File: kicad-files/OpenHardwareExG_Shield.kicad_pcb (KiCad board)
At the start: 4 copper layers, 125.1 x 59.7 mm, 195 parts, among them P1 CONN_1, P10 CONN_18, P11 CONN_1, P12 CONN_1, P13 CONN_1, P14 CONN_1, P15 CONN_1, P16 CONN_1, P17 CONN_1, P18 CONN_1, P19 ARDUINO_SHIELD, P2 CONN_1, P20 CONN_3X2, P21 CONN_3X2, P22 CONN_7, P23 CONN_1, P24 CONN_1, P25 CONN_1, P26 CONN_1, P27 CONN_1, P28 CONN_1, P29 CONN_1, P3 CONN_1, P30 CONN_1, P31 CONN_1, P32 CONN_1, P33 CONN_1, P34 CONN_1, P35 CONN_1, P36 CONN_1, P37 CONN_1, P38 CONN_1, P39 CONN_1, P4 CONN_1, P40 CONN_1, P41 CONN_1, P42 CONN_1, P43 CONN_1, P44 CONN_1, P45 CONN_1, P46 CONN_1, P47 CONN_1, P48 CONN_1, P49 CONN_1, P5 CONN_1, P50 CONN_1, P51 CONN_1, P52 CONN_1, P53 CONN_1, P54 CONN_1, P55 CONN_1, P6 CONN_1, P7 CONN_1, P8 CONN_1, P9 CONN_1, U1 ADS1299, U2 BT1308W-600D, U3 TL431BIDBZR, U4 873-AAT3220IGY-33T1, U5 ADUM6000, U6 SI8663, U7 74LS02, U8 74LS00, U9 74LS125

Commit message: add rev. 0.0 to silk screen
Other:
- board text added: "rev. 0.0"
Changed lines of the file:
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@@
     (area 59.004999 28.0083 184.7167 91.2876)
     (thickness 1.6)
-    (drawings 51)
+    (drawings 53)
     (tracks 1163)
     (zones 0)
@@
     (22 B.Mask user)
     (23 F.Mask user)
-    (24 Dwgs.User user)
-    (25 Cmts.User user)
-    (26 Eco1.User user)
-    (27 Eco2.User user)
+    (24 Dwgs.User user hide)
+    (25 Cmts.User user hide)
+    (26 Eco1.User user hide)
+    (27 Eco2.User user hide)
     (28 Edge.Cuts user)
   )
@@
     (pad_to_mask_clearance 0)
     (aux_axis_origin 0 0)
-    (visible_elements 7FFFFFBF)
+    (visible_elements 7FFFFF3F)
     (pcbplotparams
-      (layerselection 284983303)
+      (layerselection 3145728)
       (usegerberextensions true)
       (excludeedgelayer true)
@@
     )
   )
+  (gr_text "rev. 0.0" (at 154.94 78.74) (layer F.SilkS)
+    (effects (font (size 1.016 1.016) (thickness 0.2032)))
+  )
+  (gr_text "rev. 0.0" (at 154.94 78.74) (layer B.SilkS)
+    (effects (font (size 1.016 1.016) (thickness 0.2032)) (justify mirror))
+  )
   (gr_text "Licensed under CERN OHL v.1.2 or later\nhttp://ohwr.org/cernohl" (at 99.314 85.852) (layer B.SilkS)

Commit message: replace triac, new manufacture part number does not include a comma
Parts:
- U2: value BT1308W-600D -> Z0109MNT1G
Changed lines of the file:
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@@
       (effects (font (size 0.6 0.6) (thickness 0.127)))
     )
-    (fp_text value BT1308W-600D (at 0 0.762 180) (layer F.SilkS) hide
+    (fp_text value Z0109MNT1G (at 0 0.762 180) (layer F.SilkS) hide
       (effects (font (size 1.016 1.016) (thickness 0.2032)))
     )

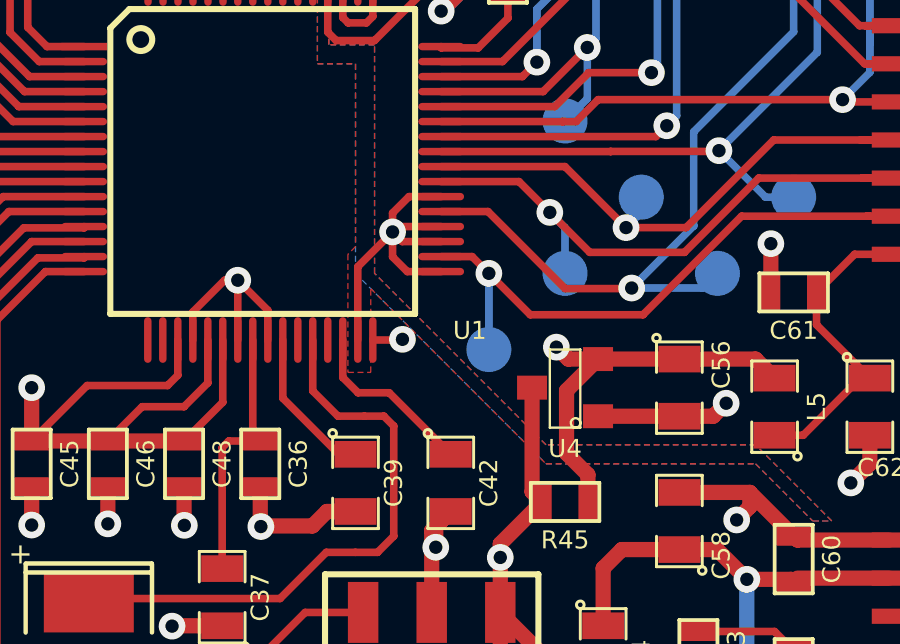
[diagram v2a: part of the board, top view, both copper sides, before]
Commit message: fixup PCB to tie ~PWDN~ and ~RESET~ to 3.3V_ISO
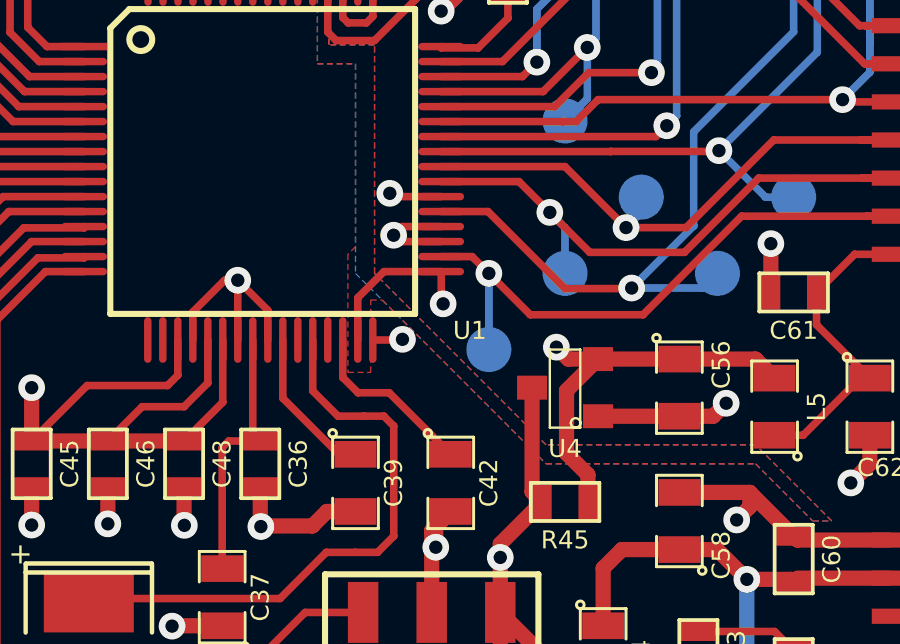
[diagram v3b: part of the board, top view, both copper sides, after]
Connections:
- U1 pad 35: AGND -> /3.3V_ISO
- U1 pad 36: AGND -> /3.3V_ISO
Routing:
- net AGND: track 162.5 -> 157.3 mm, vias 63 -> 64
- net /3.3V_ISO: track 20.2 -> 23.5 mm, vias 3 -> 4
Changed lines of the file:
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@@
     (thickness 1.6)
     (drawings 53)
-    (tracks 1163)
+    (tracks 1164)
     (zones 0)
     (modules 195)
@@
   (setup
     (last_trace_width 0.254)
+    (user_trace_width 0.254)
     (trace_clearance 0.2032)
     (zone_clearance 0.254)
@@
     (pad_to_mask_clearance 0)
     (aux_axis_origin 0 0)
-    (visible_elements 7FFFFF3F)
+    (visible_elements 7FFFF73F)
     (pcbplotparams
       (layerselection 3145728)
@@
   (net 101 N-000008)
   (net 102 N-0000080)
-  (net 103 N-0000088)
+  (net 103 N-0000087)
   (net 104 N-0000095)
   (net 105 VCC)
@@
     (add_net N-000008)
     (add_net N-0000080)
+    (add_net N-0000087)
     (add_net N-0000095)
   )
@@
     (add_net GND)
     (add_net N-00000107)
-    (add_net N-0000088)
     (add_net VCC)
   )
@@
     (pad 35 smd oval (at 2.75082 -6.0325 270) (size 0.24892 1.524)
       (layers F.Cu F.Paste F.Mask)
-      (net 57 AGND)
+      (net 4 /3.3V_ISO)
     )
     (pad 36 smd oval (at 2.25044 -6.0325 270) (size 0.24892 1.524)
       (layers F.Cu F.Paste F.Mask)
-      (net 57 AGND)
+      (net 4 /3.3V_ISO)
     )
     (pad 37 smd oval (at 1.75006 -6.0325 270) (size 0.24892 1.524)
@@
     (pad 1 smd rect (at -4.445 5.08 90) (size 0.508 1.143)
       (layers F.Cu F.Paste F.Mask)
-      (net 103 N-0000088)
+      (net 103 N-0000087)
     )
     (pad 2 smd rect (at -3.175 5.08 90) (size 0.508 1.143)
@@
     (pad 6 smd rect (at 1.905 5.08 90) (size 0.508 1.143)
       (layers F.Cu F.Paste F.Mask)
-      (net 103 N-0000088)
+      (net 103 N-0000087)
     )
     (pad 7 smd rect (at 3.175 5.08 90) (size 0.508 1.143)
       (layers F.Cu F.Paste F.Mask)
-      (net 103 N-0000088)
+      (net 103 N-0000087)
     )
     (pad 8 smd rect (at 4.445 5.08 90) (size 0.508 1.143)
@@
     (pad 1 smd rect (at -0.9525 0 90) (size 0.889 1.397)
       (layers F.Cu F.Paste F.Mask)
-      (net 103 N-0000088)
+      (net 103 N-0000087)
     )
     (pad 2 smd rect (at 0.9525 0 90) (size 0.889 1.397)
@@
     (pad 1 smd rect (at -0.9525 0 90) (size 0.889 1.397)
       (layers F.Cu F.Paste F.Mask)
-      (net 103 N-0000088)
+      (net 103 N-0000087)
     )
     (pad 2 smd rect (at 0.9525 0 90) (size 0.889 1.397)
@@
     (pad 1 smd rect (at -0.9525 0) (size 0.889 1.397)
       (layers F.Cu F.Paste F.Mask)
-      (net 103 N-0000088)
+      (net 103 N-0000087)
     )
     (pad 2 smd rect (at 0.9525 0) (size 0.889 1.397)
@@
     (pad 1 smd rect (at -0.762 0 90) (size 0.635 1.143)
       (layers F.Cu F.Paste F.Mask)
-      (net 103 N-0000088)
+      (net 103 N-0000087)
     )
     (pad 2 smd rect (at 0.762 0 90) (size 0.635 1.143)
@@
     (pad 1 smd rect (at -0.762 0 90) (size 0.635 1.143)
       (layers F.Cu F.Paste F.Mask)
-      (net 103 N-0000088)
+      (net 103 N-0000087)
     )
     (pad 2 smd rect (at 0.762 0 90) (size 0.635 1.143)
@@
   (segment (start 175.26 63.5) (end 177.8 60.96) (width 0.508) (layer B.Cu) (net 3))
   (segment (start 177.8 60.96) (end 180.34 60.96) (width 0.508) (layer B.Cu) (net 3))
+  (segment (start 100.0125 62.44082) (end 98.63582 62.44082) (width 0.254) (layer F.Cu) (net 4))
+  (segment (start 98.63582 62.44082) (end 98.425 62.23) (width 0.254) (layer F.Cu) (net 4))
+  (segment (start 100.0125 61.94044) (end 98.71456 61.94044) (width 0.254) (layer F.Cu) (net 4))
+  (via (at 98.425 62.23) (size 0.889) (layers F.Cu B.Cu) (net 4))
+  (segment (start 98.71456 61.94044) (end 98.425 62.23) (width 0.254) (layer F.Cu) (net 4))
   (segment (start 106.68 48.5775) (end 106.68 47.74) (width 0.508) (layer F.Cu) (net 4))
   (via (at 106.04 47.1) (size 0.889) (layers F.Cu B.Cu) (net 4))
@@
   (segment (start 167.64 48.26) (end 161.925 48.26) (width 0.254) (layer F.Cu) (net 56))
   (segment (start 168.275 48.895) (end 167.64 48.26) (width 0.254) (layer F.Cu) (net 56))
+  (segment (start 100.0125 60.94222) (end 98.40722 60.94222) (width 0.254) (layer F.Cu) (net 57))
+  (via (at 98.298 60.833) (size 0.889) (layers F.Cu B.Cu) (net 57))
+  (segment (start 98.40722 60.94222) (end 98.298 60.833) (width 0.254) (layer F.Cu) (net 57))
+  (segment (start 100.0125 63.44158) (end 100.0125 64.4525) (width 0.254) (layer F.Cu) (net 57))
+  (via (at 100.076 64.516) (size 0.889) (layers F.Cu B.Cu) (net 57))
+  (segment (start 100.0125 64.4525) (end 100.076 64.516) (width 0.254) (layer F.Cu) (net 57))
+  (segment (start 100.0125 63.44158) (end 98.10242 63.44158) (width 0.254) (layer F.Cu) (net 57))
+  (segment (start 97.2312 64.3128) (end 97.2312 65.7225) (width 0.254) (layer F.Cu) (net 57))
+  (segment (start 98.10242 63.44158) (end 97.2312 64.3128) (width 0.254) (layer F.Cu) (net 57))
   (segment (start 109.22 44.63) (end 109.22 41.91) (width 0.508) (layer F.Cu) (net 57))
   (segment (start 114.3 39.095) (end 114.3 36.83) (width 0.508) (layer B.Cu) (net 57))
@@
   (segment (start 96.91 55.15) (end 97.52 55.15) (width 0.254) (layer F.Cu) (net 57))
   (segment (start 96.73082 54.97082) (end 96.91 55.15) (width 0.254) (layer F.Cu) (net 57))
-  (segment (start 100.0125 63.44158) (end 98.88158 63.44158) (width 0.254) (layer F.Cu) (net 57))
-  (via (at 98.39 62.12) (size 0.889) (layers F.Cu B.Cu) (net 57))
-  (segment (start 98.39 62.95) (end 98.39 62.12) (width 0.254) (layer F.Cu) (net 57))
-  (segment (start 98.88158 63.44158) (end 98.39 62.95) (width 0.254) (layer F.Cu) (net 57))
-  (segment (start 97.2312 65.7225) (end 97.2312 63.2788) (width 0.254) (layer F.Cu) (net 57))
-  (segment (start 97.2312 63.2788) (end 98.39 62.12) (width 0.254) (layer F.Cu) (net 57))
-  (segment (start 100.0125 60.94222) (end 98.93778 60.94222) (width 0.254) (layer F.Cu) (net 57))
-  (segment (start 98.39 61.49) (end 98.39 62.12) (width 0.254) (layer F.Cu) (net 57))
-  (segment (start 98.93778 60.94222) (end 98.39 61.49) (width 0.254) (layer F.Cu) (net 57))
-  (segment (start 100.0125 62.44082) (end 98.71082 62.44082) (width 0.254) (layer F.Cu) (net 57))
-  (segment (start 98.56956 61.94044) (end 98.39 62.12) (width 0.254) (layer F.Cu) (net 57))
-  (segment (start 98.56956 61.94044) (end 100.0125 61.94044) (width 0.254) (layer F.Cu) (net 57))
-  (segment (start 98.71082 62.44082) (end 98.39 62.12) (width 0.254) (layer F.Cu) (net 57))
   (segment (start 128.27 72.263) (end 128.651 72.644) (width 0.508) (layer F.Cu) (net 58))
   (segment (start 128.651 72.644) (end 132.08 72.644) (width 0.508) (layer F.Cu) (net 58))
@@
         (xy 100.33 47.625) (xy 97.79 50.165) (xy 97.79 51.435) (xy 95.885 53.34) (xy 95.885 56.515)
         (xy 97.155 56.515) (xy 97.155 62.611) (xy 96.901 62.865) (xy 96.901 66.802) (xy 97.663 66.802)
-        (xy 97.663 64.008) (xy 103.505 69.85) (xy 110.49 69.85) (xy 112.395 71.755) (xy 113.03 71.755)
-        (xy 110.49 69.215) (xy 103.505 69.215) (xy 97.79 63.5) (xy 97.79 55.88) (xy 96.266 55.88)
-        (xy 96.266 53.594) (xy 98.425 51.435) (xy 98.425 50.165) (xy 100.33 48.26) (xy 102.87 48.26)
-        (xy 104.14 46.99) (xy 104.14 40.64) (xy 100.33 40.64) (xy 99.695 41.275) (xy 91.44 41.275)
-        (xy 90.805 40.64) (xy 90.805 36.83) (xy 109.855 36.83) (xy 109.855 42.545) (xy 115.57 42.545)
+        (xy 97.663 64.389) (xy 98.044 64.389) (xy 103.505 69.85) (xy 110.49 69.85) (xy 112.395 71.755)
+        (xy 113.03 71.755) (xy 110.49 69.215) (xy 103.505 69.215) (xy 97.79 63.5) (xy 97.79 55.88)
+        (xy 96.266 55.88) (xy 96.266 53.594) (xy 98.425 51.435) (xy 98.425 50.165) (xy 100.33 48.26)
+        (xy 102.87 48.26) (xy 104.14 46.99) (xy 104.14 40.64) (xy 100.33 40.64) (xy 99.695 41.275)
+        (xy 91.44 41.275) (xy 90.805 40.64) (xy 90.805 36.83) (xy 109.855 36.83) (xy 109.855 42.545)
+        (xy 115.57 42.545)
       )
     )

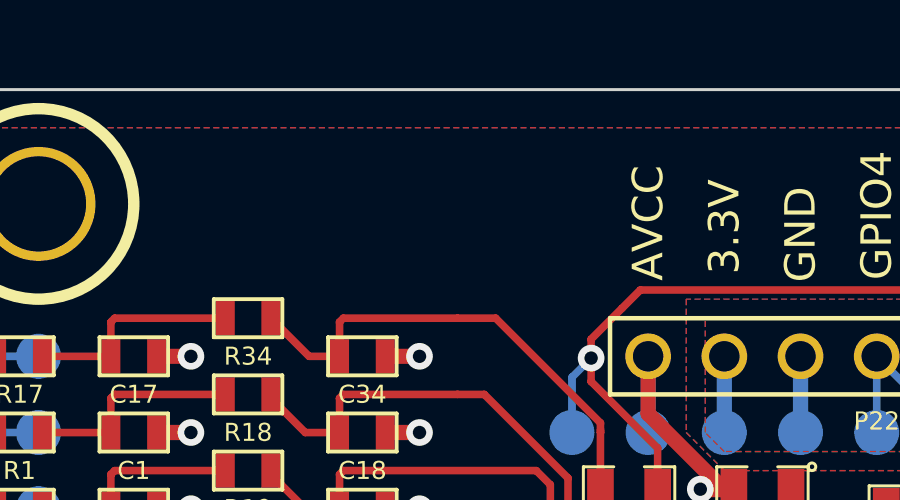
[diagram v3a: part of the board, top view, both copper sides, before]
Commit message: just drop C73 on the pcb, will need layout work
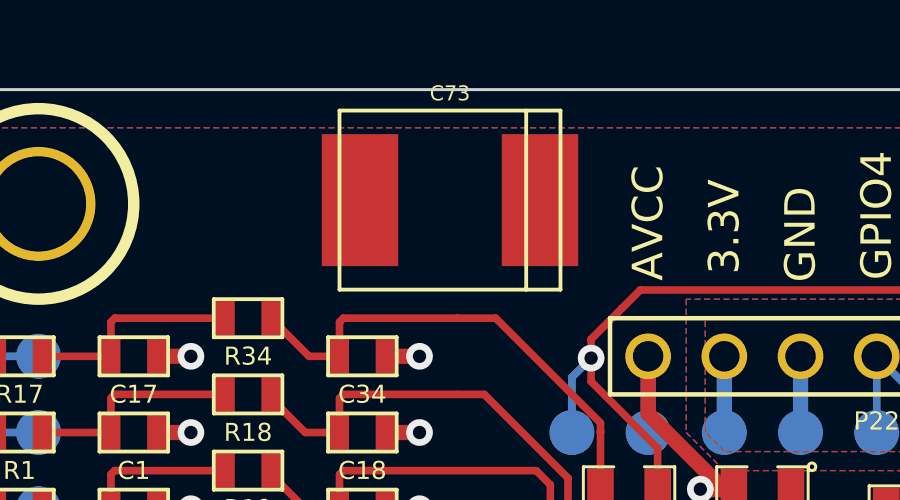
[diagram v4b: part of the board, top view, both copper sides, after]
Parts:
- added C73: 330uF, c_tant_E, F.Cu at (82.3, 32.9)
- C43: value 10uF -> 100nF
